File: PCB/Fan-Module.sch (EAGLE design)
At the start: 27 parts, among them U1 ATSAMD11C14A-SSUT_ATSAMD11C14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, U3 LDL1117S12R_LDL1117S12R

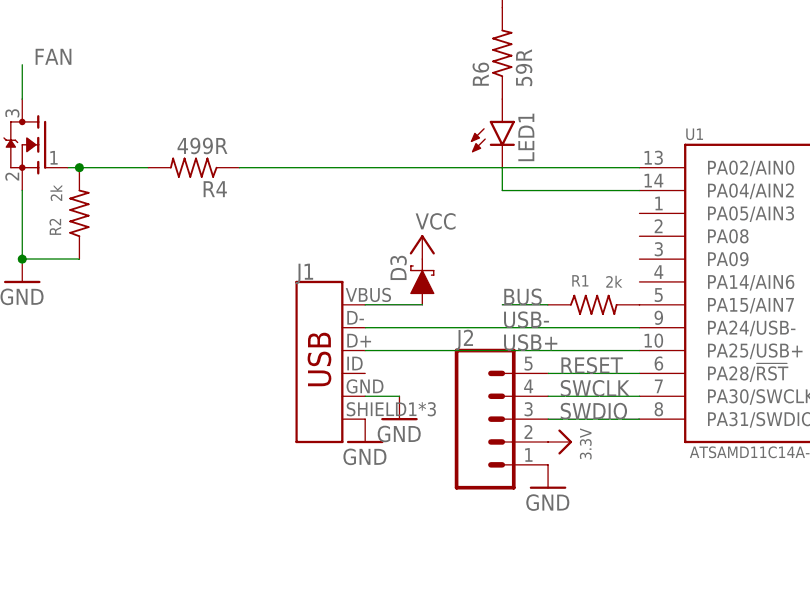
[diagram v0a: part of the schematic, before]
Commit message: added 4pin connector for remaining pins on all boards
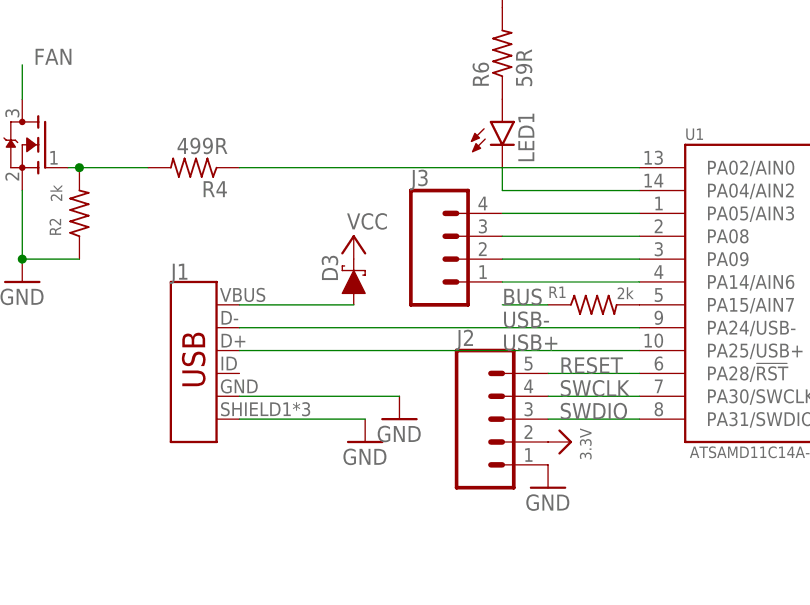
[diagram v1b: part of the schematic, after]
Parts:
- added J3: (no value), SparkFun-Connectors:CONN_04PTH
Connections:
- new net N$10: J3.2, U1.PA09
- new net N$11: J3.1, U1.PA14/AIN6
- new net N$7: J3.4, U1.PA05/AIN3
- new net N$9: J3.3, U1.PA08
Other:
- moved on the sheet: D3, J1
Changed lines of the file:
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@@
 <?xml version="1.0" encoding="utf-8"?>
 <!DOCTYPE eagle SYSTEM "eagle.dtd">
-<eagle version="9.3.0">
+<eagle version="9.2.2">
 <drawing>
 <settings>
@@
 <part name="U1" library="LED-Board" deviceset="ATSAMD11C14A-SSUT_ATSAMD11C14A-SSUT" device=""/>
 <part name="R4" library="rcl" library_urn="urn:adsk.eagle:library:334" deviceset="R-US_" device="R0805" package3d_urn="urn:adsk.eagle:package:23553/2" value="499R"/>
+<part name="J3" library="SparkFun-Connectors" deviceset="CONN_04" device="PTH"/>
 </parts>
 <sheets>
@@
 <attribute name="SHEET" x="116.205" y="-76.2" size="2.54" layer="94"/>
 </instance>
-<instance part="J1" gate="J1" x="-71.12" y="30.48" smashed="yes">
-<attribute name="VALUE" x="-73.66" y="20.574" size="1.778" layer="96" font="vector" rot="MR180" align="top-left"/>
-<attribute name="NAME" x="-73.66" y="40.894" size="1.778" layer="95" font="vector"/>
+<instance part="J1" gate="J1" x="-85.09" y="30.48" smashed="yes">
+<attribute name="VALUE" x="-87.63" y="20.574" size="1.778" layer="96" font="vector" rot="MR180" align="top-left"/>
+<attribute name="NAME" x="-87.63" y="40.894" size="1.778" layer="95" font="vector"/>
 </instance>
 <instance part="J2" gate="G$1" x="-53.34" y="25.4" smashed="yes">
@@
 </instance>
 <instance part="R1" gate="G$1" x="-40.64" y="38.1" smashed="yes">
-<attribute name="NAME" x="-43.18" y="40.132" size="1.27" layer="95" font="vector"/>
-<attribute name="VALUE" x="-39.37" y="40.005" size="1.27" layer="96" font="vector"/>
+<attribute name="NAME" x="-45.72" y="38.862" size="1.27" layer="95" font="vector"/>
+<attribute name="VALUE" x="-38.1" y="38.735" size="1.27" layer="96" font="vector"/>
 </instance>
 <instance part="R6" gate="G$1" x="-50.8" y="66.04" smashed="yes" rot="R90">
@@
 <attribute name="VALUE" x="-48.26" y="15.24" size="1.778" layer="96"/>
 </instance>
-<instance part="D3" gate="G$1" x="-59.69" y="40.64" smashed="yes" rot="R90">
-<attribute name="NAME" x="-61.4426" y="40.64" size="1.778" layer="95" rot="R90"/>
-</instance>
-<instance part="P+1" gate="VCC" x="-59.69" y="45.72" smashed="yes">
-<attribute name="VALUE" x="-55.88" y="48.26" size="1.778" layer="96" rot="R180"/>
+<instance part="D3" gate="G$1" x="-67.31" y="40.64" smashed="yes" rot="R90">
+<attribute name="NAME" x="-69.0626" y="40.64" size="1.778" layer="95" rot="R90"/>
+</instance>
+<instance part="P+1" gate="VCC" x="-67.31" y="45.72" smashed="yes">
+<attribute name="VALUE" x="-63.5" y="48.26" size="1.778" layer="96" rot="R180"/>
 </instance>
 <instance part="F1" gate="G$1" x="-1.27" y="0" smashed="yes">
@@
 <attribute name="NAME" x="-81.28" y="51.8414" size="1.778" layer="95" rot="R180"/>
 <attribute name="VALUE" x="-81.28" y="56.642" size="1.778" layer="96" rot="R180"/>
+</instance>
+<instance part="J3" gate="J1" x="-55.88" y="43.18" smashed="yes">
+<attribute name="VALUE" x="-60.96" y="35.814" size="1.778" layer="96" font="vector"/>
+<attribute name="NAME" x="-60.96" y="51.308" size="1.778" layer="95" font="vector"/>
 </instance>
 </instances>
@@
 <pinref part="J1" gate="J1" pin="SHIELD"/>
 <pinref part="GND4" gate="1" pin="GND"/>
+<wire x1="-80.01" y1="25.4" x2="-66.04" y2="25.4" width="0.1524" layer="91"/>
 </segment>
 <segment>
 <pinref part="GND7" gate="1" pin="GND"/>
 <pinref part="J1" gate="J1" pin="GND"/>
-<wire x1="-62.23" y1="27.94" x2="-66.04" y2="27.94" width="0.1524" layer="91"/>
+<wire x1="-62.23" y1="27.94" x2="-80.01" y2="27.94" width="0.1524" layer="91"/>
 </segment>
 <segment>
@@
 <segment>
 <pinref part="J1" gate="J1" pin="D-"/>
-<wire x1="-35.56" y1="35.56" x2="-66.04" y2="35.56" width="0.1524" layer="91"/>
+<wire x1="-35.56" y1="35.56" x2="-80.01" y2="35.56" width="0.1524" layer="91"/>
 <label x="-50.8" y="35.56" size="1.778" layer="95"/>
 <pinref part="U1" gate="G$1" pin="PA24/USB-"/>
@@
 <segment>
 <pinref part="J1" gate="J1" pin="D+"/>
-<wire x1="-35.56" y1="33.02" x2="-66.04" y2="33.02" width="0.1524" layer="91"/>
+<wire x1="-35.56" y1="33.02" x2="-80.01" y2="33.02" width="0.1524" layer="91"/>
 <label x="-50.8" y="33.02" size="1.778" layer="95"/>
 <pinref part="U1" gate="G$1" pin="PA25/USB+"/>
@@
 <pinref part="J1" gate="J1" pin="VBUS"/>
 <pinref part="D3" gate="G$1" pin="A"/>
-<wire x1="-66.04" y1="38.1" x2="-59.69" y2="38.1" width="0.1524" layer="91"/>
+<wire x1="-80.01" y1="38.1" x2="-67.31" y2="38.1" width="0.1524" layer="91"/>
 </segment>
 </net>
@@
 </segment>
 </net>
+<net name="N$7" class="0">
+<segment>
+<pinref part="J3" gate="J1" pin="4"/>
+<pinref part="U1" gate="G$1" pin="PA05/AIN3"/>
+<wire x1="-50.8" y1="48.26" x2="-35.56" y2="48.26" width="0.1524" layer="91"/>
+</segment>
+</net>
+<net name="N$9" class="0">
+<segment>
+<pinref part="U1" gate="G$1" pin="PA08"/>
+<pinref part="J3" gate="J1" pin="3"/>
+<wire x1="-35.56" y1="45.72" x2="-50.8" y2="45.72" width="0.1524" layer="91"/>
+</segment>
+</net>
+<net name="N$10" class="0">
+<segment>
+<pinref part="J3" gate="J1" pin="2"/>
+<pinref part="U1" gate="G$1" pin="PA09"/>
+<wire x1="-50.8" y1="43.18" x2="-35.56" y2="43.18" width="0.1524" layer="91"/>
+</segment>
+</net>
+<net name="N$11" class="0">
+<segment>
+<pinref part="U1" gate="G$1" pin="PA14/AIN6"/>
+<pinref part="J3" gate="J1" pin="1"/>
+<wire x1="-35.56" y1="40.64" x2="-50.8" y2="40.64" width="0.1524" layer="91"/>
+</segment>
+</net>
